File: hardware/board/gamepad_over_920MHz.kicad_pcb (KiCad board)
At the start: 2 copper layers, 90 x 50 mm, 8 parts, among them J1 PinHeader_1x04_P2.54mm_Vertic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, U1 XIAO_RP2040, U2 IM920sL_ADP

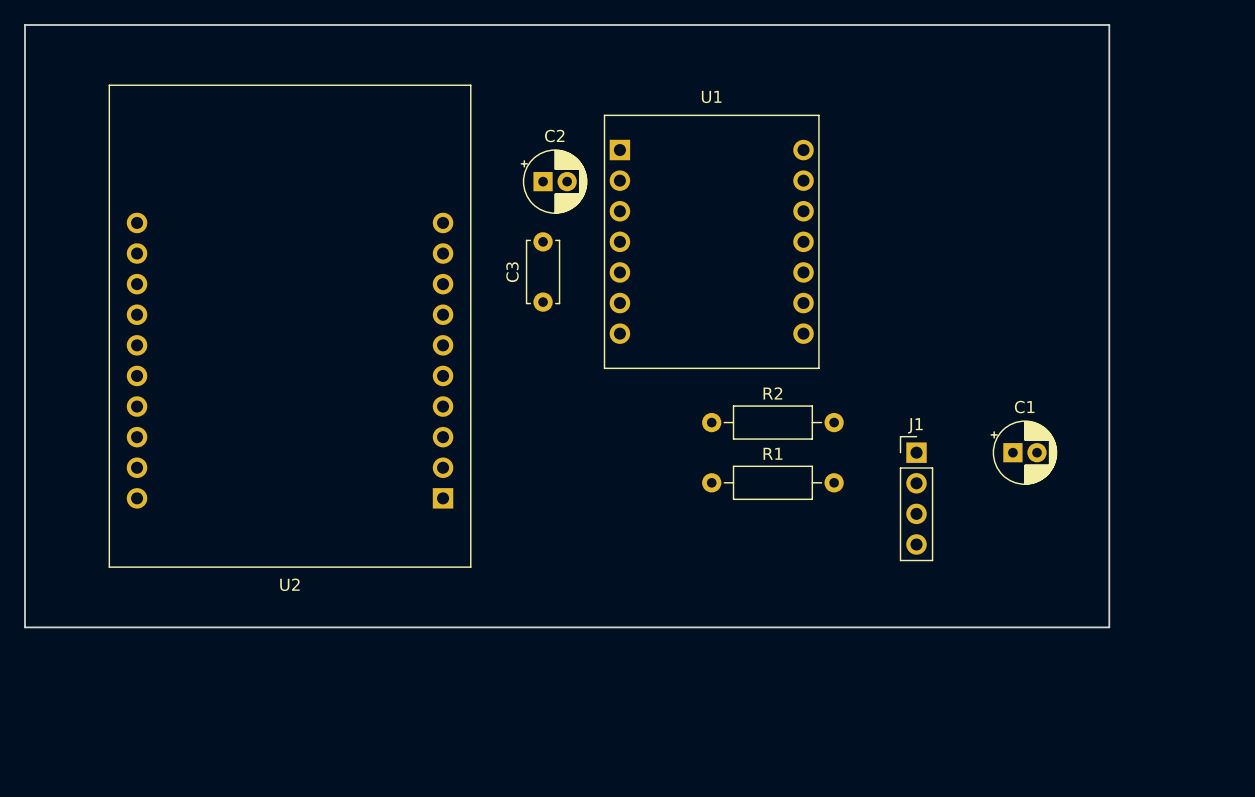
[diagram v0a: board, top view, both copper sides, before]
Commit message: 基板を配線し、GND ベタと四隅の固定穴を追加（DRC 0 violations）
- 全 11 ネットを配線。D+ は表面、D− は裏面（XIAO 側と J1 側で
  D+/D− の上下が逆転しており 1 層では必ず交差するため）
- 両面 GND ベタ。左上 22x20mm はアンテナ用に銅を抜いた
- 四隅に φ3.2（M3）の固定穴を追加。外形を 100x62mm に拡大
- J1 のシェル固定パッドを GND に接続
- 確認用に表面・裏面の PDF を個別出力

Co-Authored-By: Claude Opus 5 (1M context) <noreply@anthropic.com>
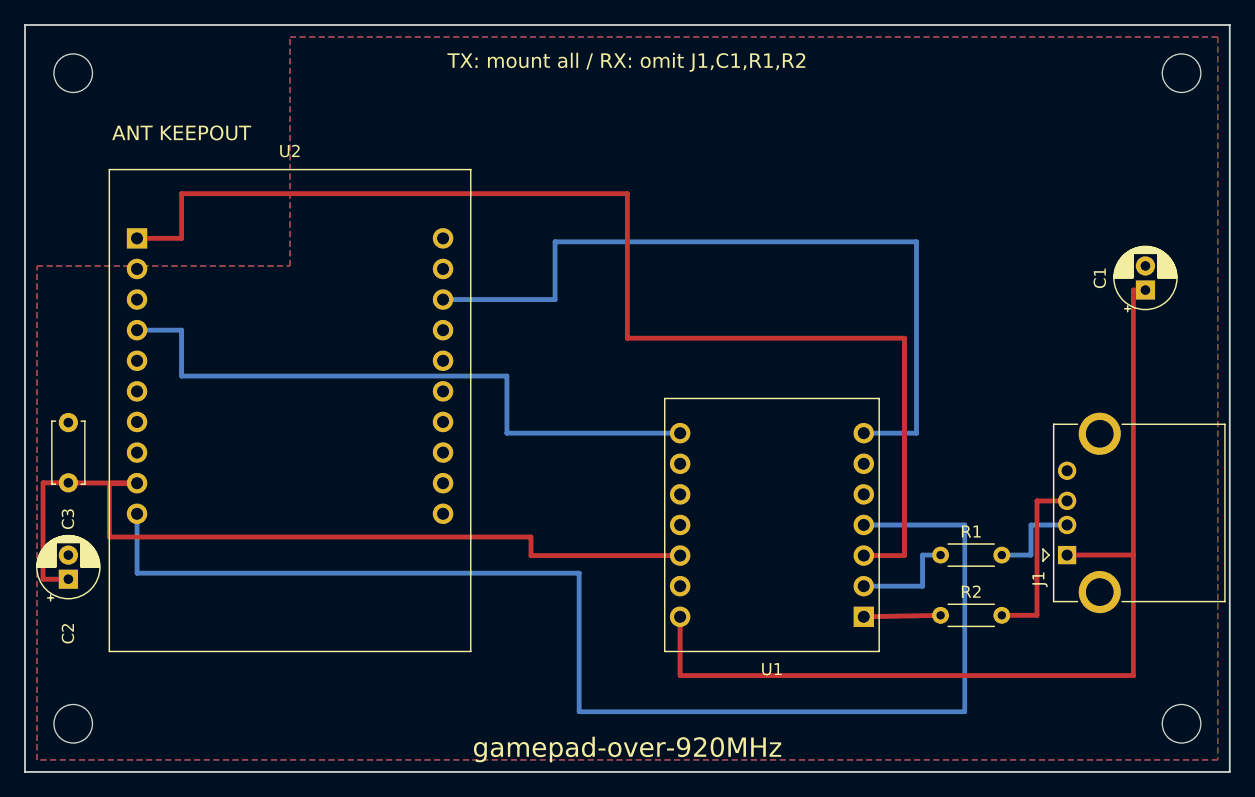
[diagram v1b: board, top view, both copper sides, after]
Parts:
- removed the C3 at (43.0, 23.0)
- added C2: CP_Radial_D5.0mm_P2.00mm, CP_Radial_D5.0mm_P2.00mm, F.Cu at (3.60, 46.0)
- added H1: MountingHole_3.2mm_M3, MountingHole_3.2mm_M3, F.Cu at (4.00, 4.00)
- added H2: MountingHole_3.2mm_M3, MountingHole_3.2mm_M3, F.Cu at (96.0, 4.00)
- added H3: MountingHole_3.2mm_M3, MountingHole_3.2mm_M3, F.Cu at (4.00, 58.0)
- added H4: MountingHole_3.2mm_M3, MountingHole_3.2mm_M3, F.Cu at (96.0, 58.0)
- C3: renamed from C2; value CP_Radial_D5.0mm_P2.00mm -> C_Disc_D5.0mm_W2.5mm_P5.00mm; footprint CP_Radial_D5.0mm_P2.00mm -> C_Disc_D5.0mm_W2.5mm_P5.00mm
- J1: value PinHeader_1x04_P2.54mm_Vertical -> USB_A_CONNFLY_DS1095-WNR0; footprint PinHeader_1x04_P2.54mm_Vertical -> USB_A_CONNFLY_DS1095-WNR0
- R1, R2: value R_Axial_DIN0207_L6.3mm_D2.5mm_P10.16mm_Horizontal -> R_Axial_DIN0204_L3.6mm_D1.6mm_P5.08mm_Horizontal; footprint R_Axial_DIN0207_L6.3mm_D2.5mm_P10.16mm_Horizontal -> R_Axial_DIN0204_L3.6mm_D1.6mm_P5.08mm_Horizontal
- moved C3 46.7 mm to (3.60, 38.0), turned to 90 degrees
- moved R2 24.8 mm to (76.0, 49.0)
- moved U1 24.0 mm to (62.0, 41.5), turned to 180 degrees
- moved R1 19.9 mm to (76.0, 44.0)
- moved C1 17.4 mm to (93.0, 22.0), turned to 90 degrees
- moved J1 15.1 mm to (86.5, 44.0), turned to 90 degrees
- moved U2 7.00 mm to (22.0, 32.0), turned to 0 degrees
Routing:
- net IM_RESET: track 0.00 -> 109.0 mm
- net IM_BUSY: track 0.00 -> 100.8 mm
- net +5V: track 0.00 -> 81.0 mm
- net +3V3: track 0.00 -> 73.6 mm
- net IM_RXD: track 0.00 -> 64.3 mm
- net IM_TXD: track 0.00 -> 53.6 mm
- net USB_DP_CON: track 0.00 -> 14.9 mm
- net USB_DM: track 0.00 -> 8.96 mm
- net USB_DM_CON: track 0.00 -> 7.92 mm
- net USB_DP: track 0.00 -> 6.38 mm
- added copper zone on B.Cu, net GND
- added copper zone on F.Cu, net GND
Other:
- board size 90 x 50 mm -> 100 x 62 mm
- board text added: "ANT KEEPOUT"
- board text added: "TX: mount all / RX: omit J1,C1,R1,R2"
- board text added: "gamepad-over-920MHz"
